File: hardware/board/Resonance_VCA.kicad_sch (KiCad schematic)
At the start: 33 parts

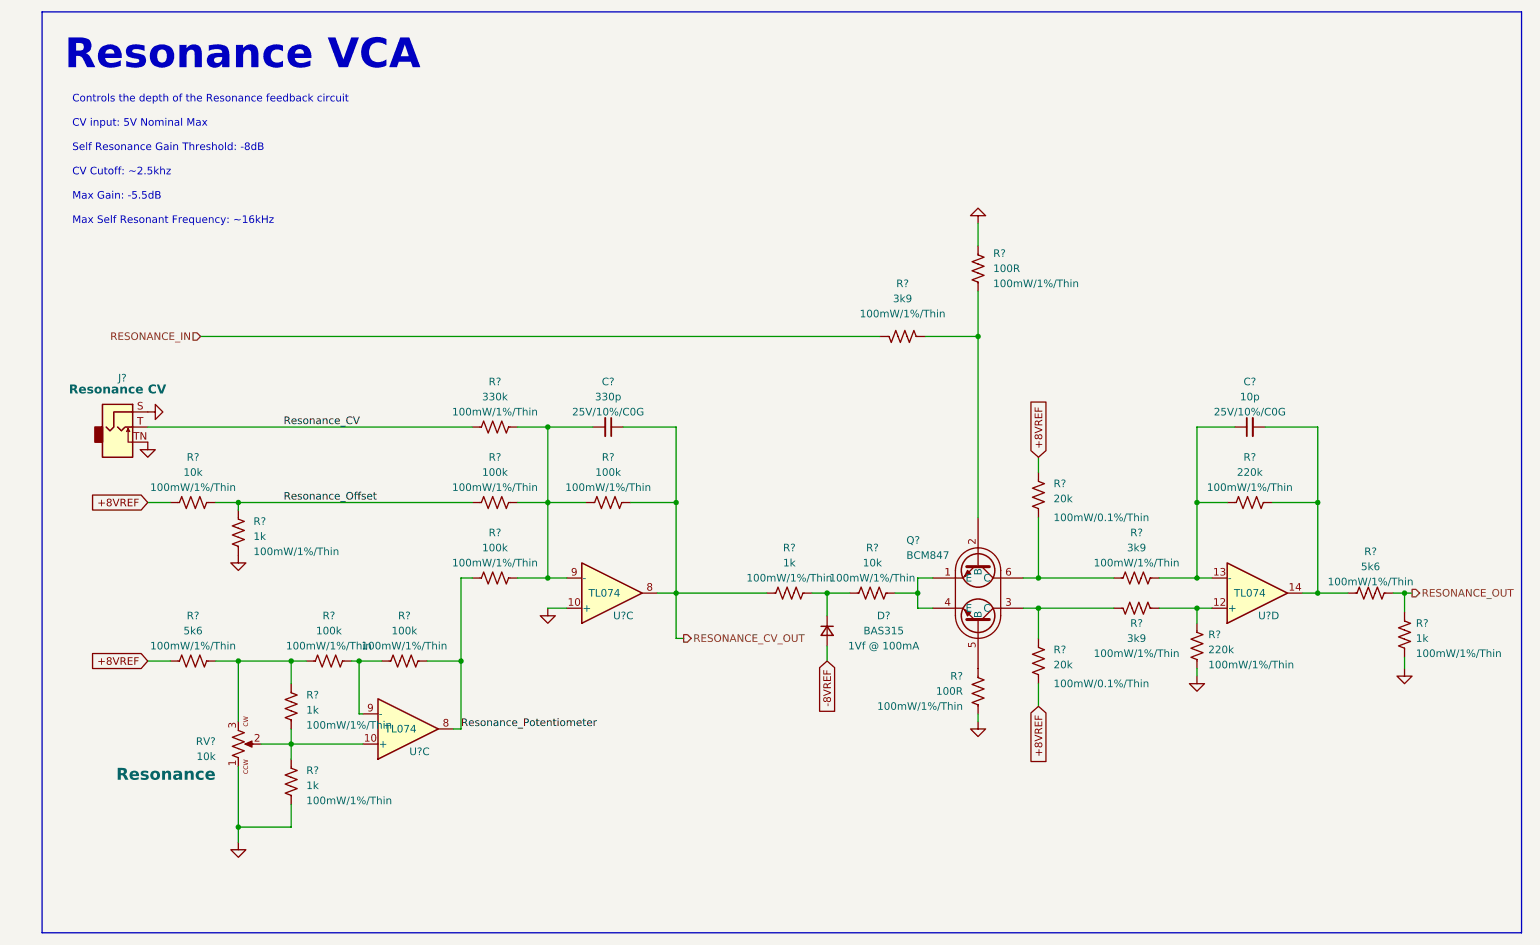
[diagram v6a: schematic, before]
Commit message: hardware: update schematic fonts/text sizes, some slight readability improvements
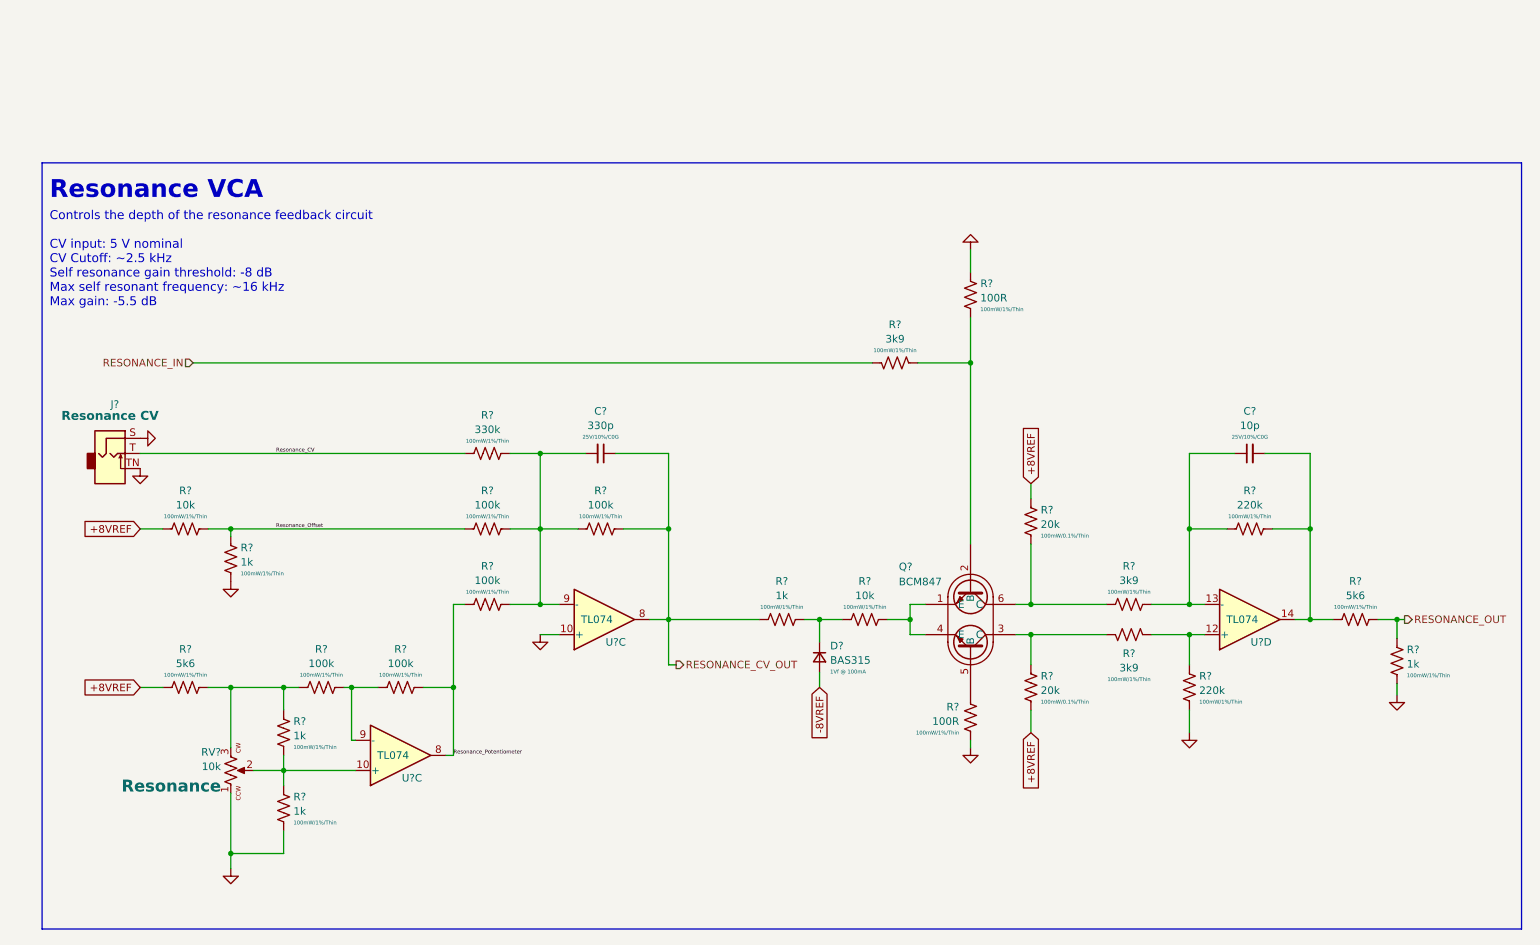
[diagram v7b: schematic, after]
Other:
- note added: "Controls the depth of the resonance feedback circuit CV input: 5 V nominal CV Cutoff: ~2.5 kHz Self resonance gain threshold: -8 dB Max self resonant frequency: ~16 kHz Max gain: -5.5 dB"
- note removed: "Controls the depth of the Resonance feedback circuit CV input: 5V Nominal Max Self Resonance Gain Threshold: -8dB CV Cutoff: ~2.5khz Max Gain: -5.5dB Max Self Resonant Frequency: ~16kHz"
- moved on the sheet: C?, D?, J?, Q?, R?, RV?, U?C, U?D

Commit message: hardware: use new Winterbloom sheet layout
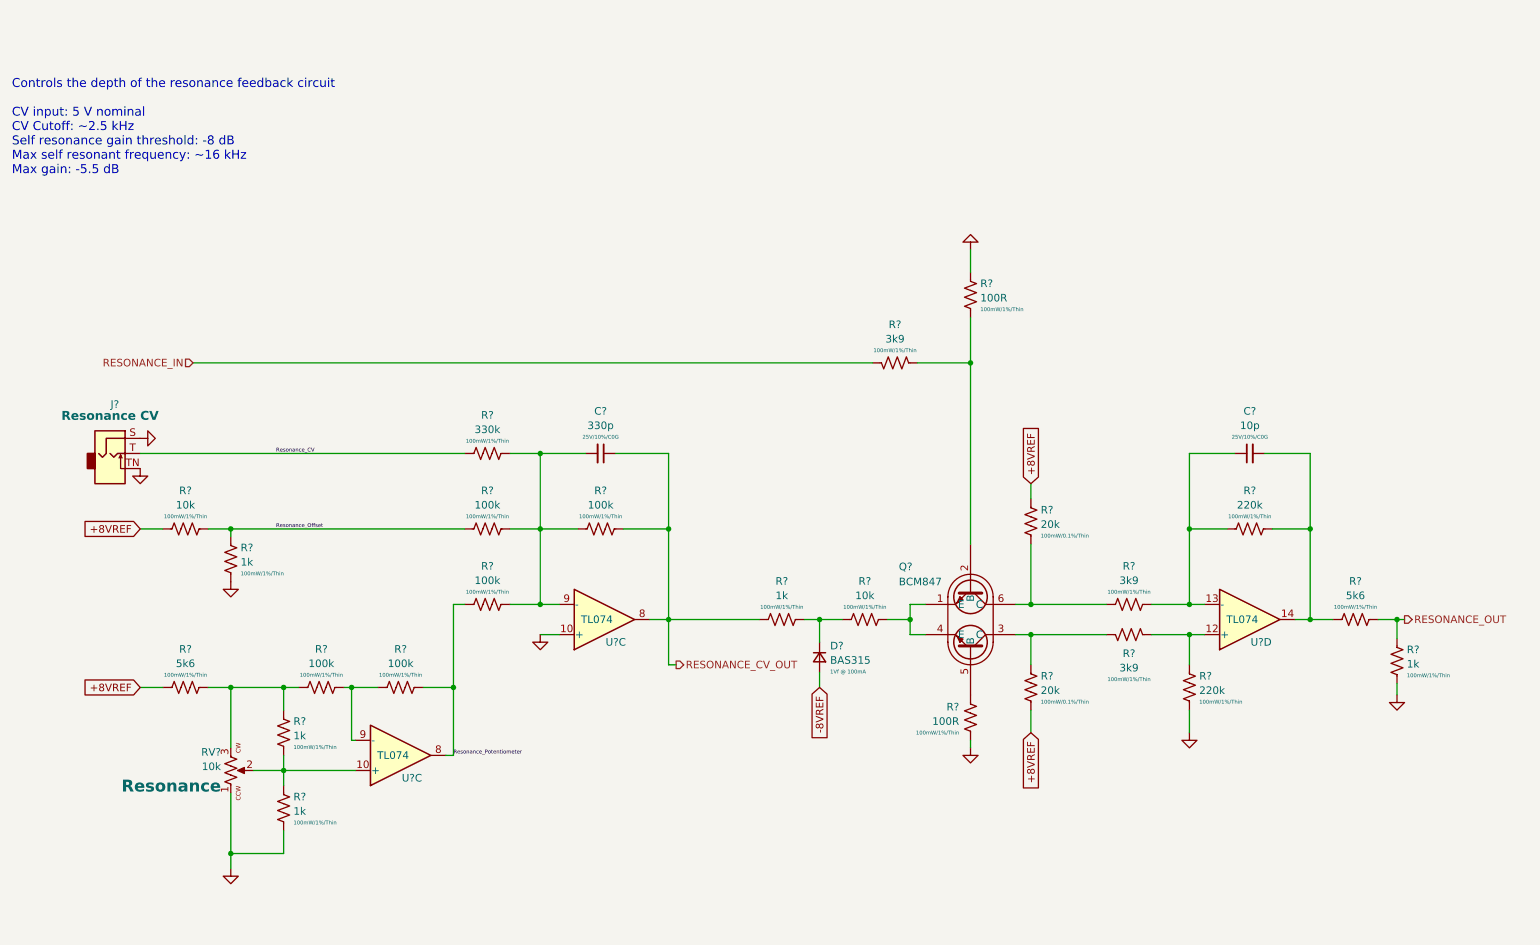
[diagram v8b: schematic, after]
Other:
- note removed: "Resonance VCA"
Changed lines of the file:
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@@
     (stroke (width 0) (type default))
   )
-  (rectangle (start 15.24 40.64) (end 264.16 169.545)
-    (stroke (width 0) (type default))
-    (fill (type none))
-  )
-  (text "Resonance VCA" (at 16.51 46.99 0)
-    (effects (font (face "Space Grotesk") (size 3 3) (thickness 0.508) bold) (justify left bottom))
-  )
   (text "Controls the depth of the resonance feedback circuit \n\nCV input: 5 V nominal\nCV Cutoff: ~2.5 kHz\nSelf resonance gain threshold: -8 dB\nMax self resonant frequency: ~16 kHz\nMax gain: -5.5 dB\n\n\n"
-    (at 16.51 69.85 0)
+    (at 10.16 47.625 0)
     (effects (font (face "Nunito") (size 1.5 1.5)) (justify left bottom))
   )
